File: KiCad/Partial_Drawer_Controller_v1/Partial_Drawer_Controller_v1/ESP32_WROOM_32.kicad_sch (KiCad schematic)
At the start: 41 parts, among them Q1 SS8050, Q2 2N7002T-7-F, Q3 2N7002T-7-F, Q5 SS8050, U6 CP2102N-Axx-xQFN28, U7 ESP32-WROOM-32E-N8, X1 USB-Micro

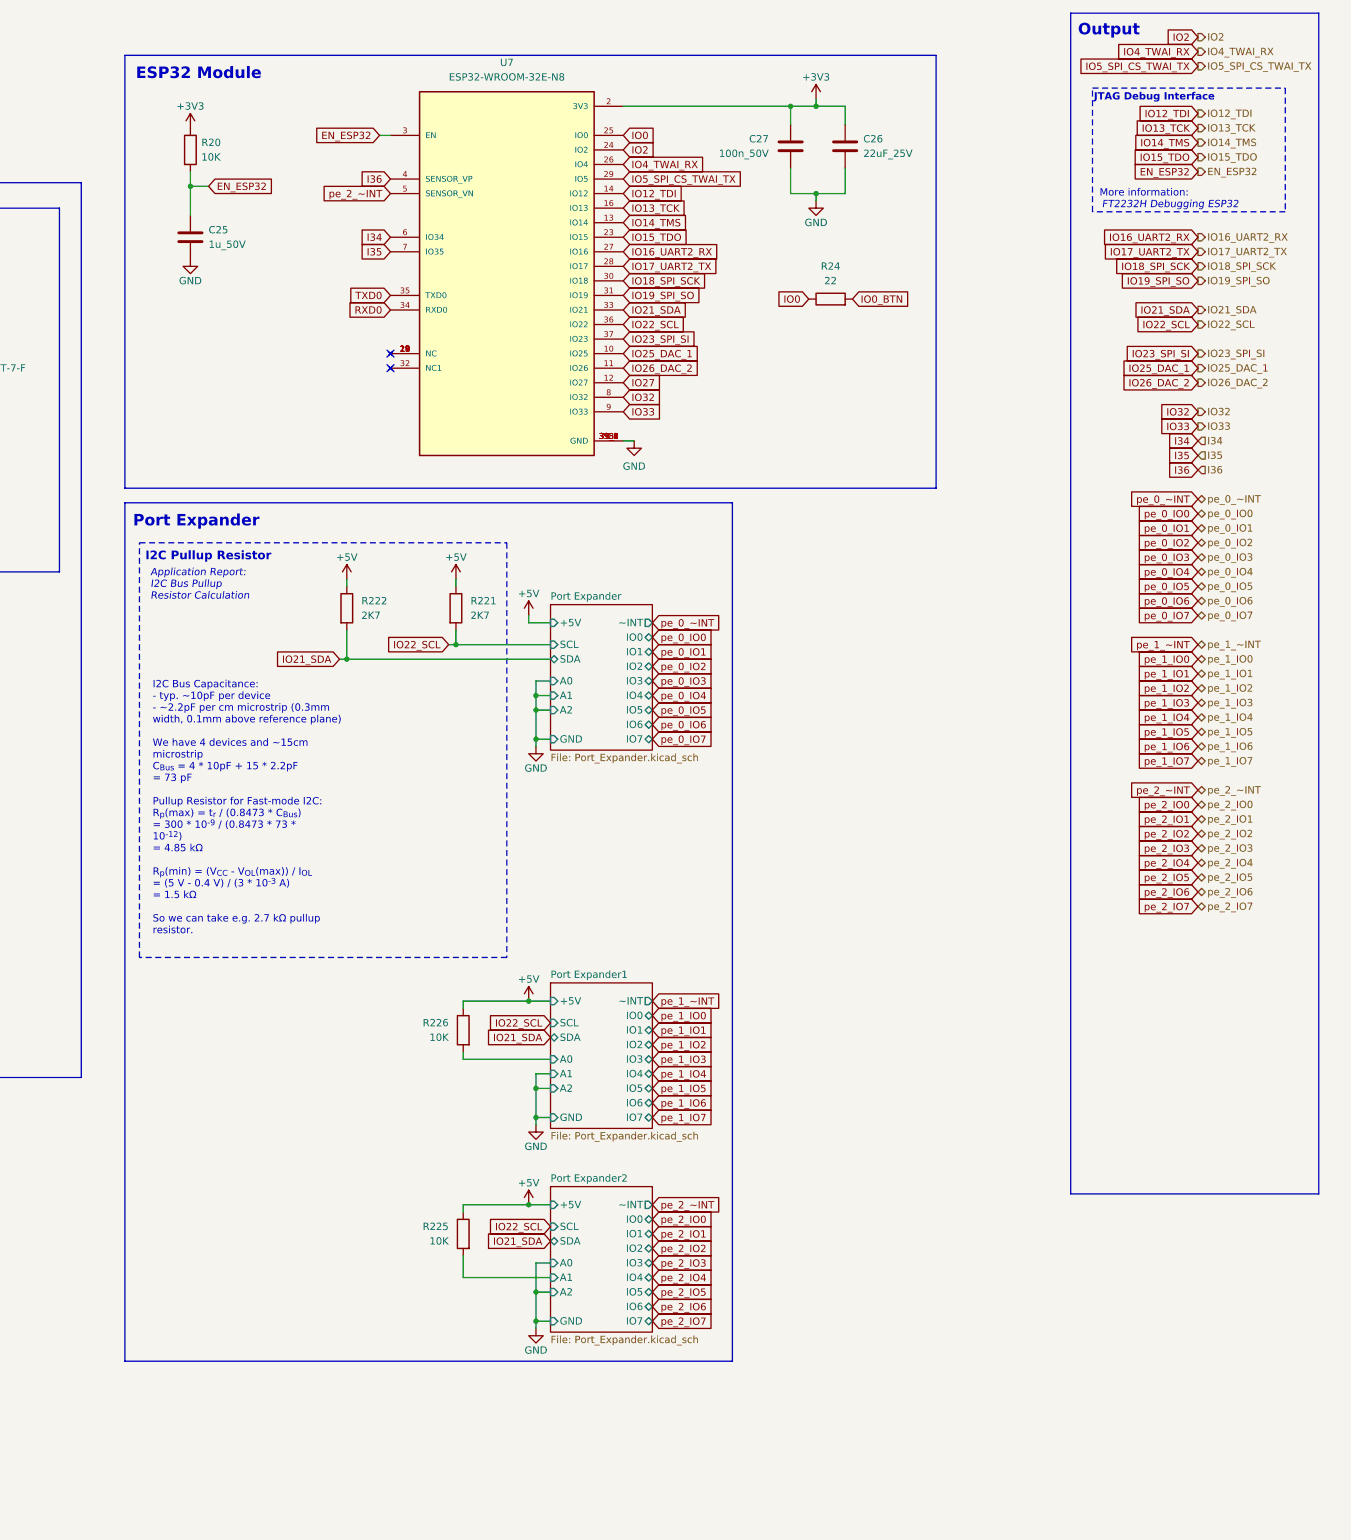
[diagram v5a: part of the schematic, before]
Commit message: feat: adds a lot of connectors and e-drawer support
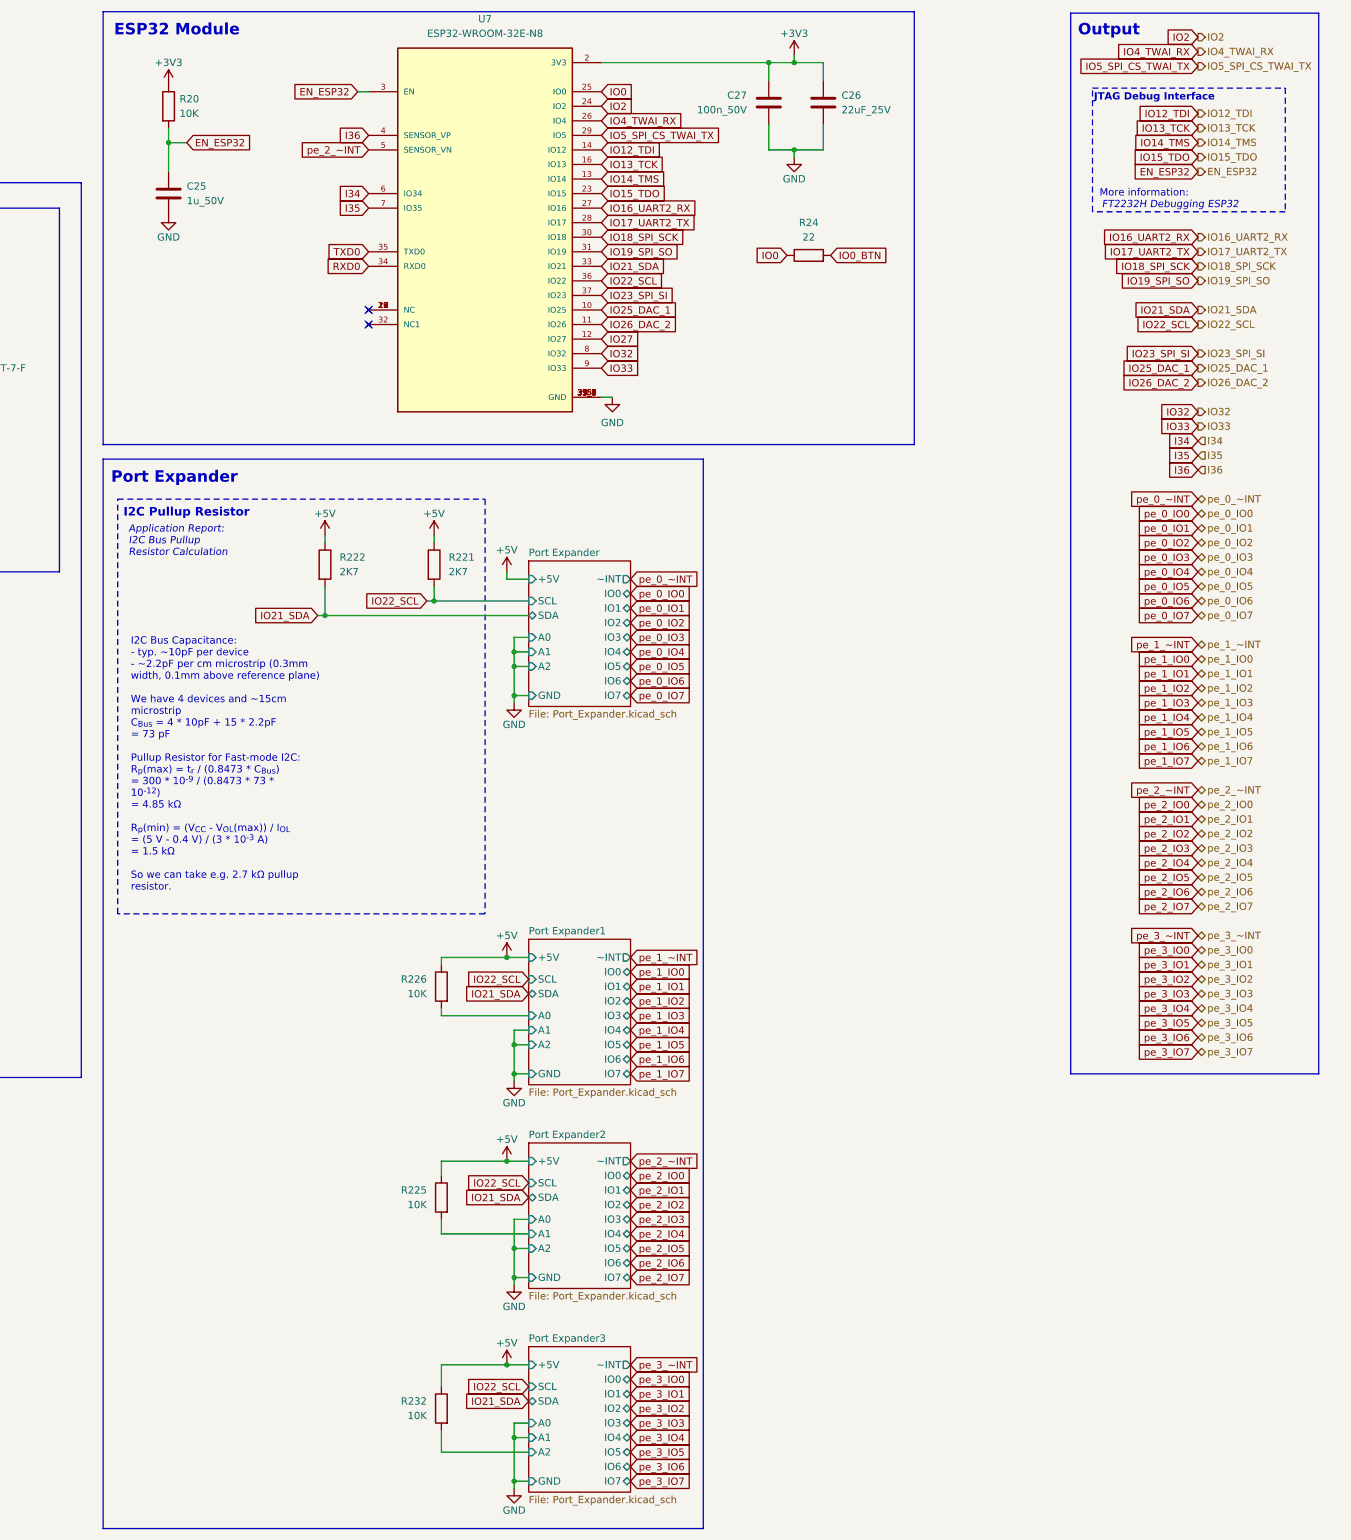
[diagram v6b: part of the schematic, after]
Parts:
- added R232: 10K, Resistor_SMD:R_0402_1005Metric, symbol _R_0402:10K
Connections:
- net +5V: now also R232.1
- new net Port Expander3/A2: R232.2
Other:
- added sheet Port Expander3 (Port_Expander.kicad_sch)
- moved on the sheet: C25, C26, C27, R20, R221, R222, R225, R226, R24, U7

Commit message: feat: finishing first draft for `partial_drawer_controller_v1` schematic
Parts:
- removed R226, R232: 10K, Resistor_SMD:R_0402_1005Metric, symbol _R_0402:10K
- added R224: 10K, Resistor_SMD:R_0402_1005Metric, symbol _R_0402:10K
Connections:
- net +5V: now also R224.1
- net Port Expander1/A0: now also R224.2
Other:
- removed sheet Port Expander3
- sheet Port Expander ports: added IO0_0, IO0_1, IO0_2, IO0_3, IO0_4, IO0_5, IO0_6, IO0_7, IO1_0, IO1_1, IO1_2, IO1_3, IO1_4, IO1_5, IO1_6, IO1_7; removed IO0, IO1, IO2, IO3, IO4, IO5, IO6, IO7
- sheet Port Expander1 ports: added IO0_0, IO0_1, IO0_2, IO0_3, IO0_4, IO0_5, IO0_6, IO0_7, IO1_0, IO1_1, IO1_2, IO1_3, IO1_4, IO1_5, IO1_6, IO1_7; removed IO0, IO1, IO2, IO3, IO4, IO5, IO6, IO7
- sheet Port Expander2 ports: added IO0_0, IO0_1, IO0_2, IO0_3, IO0_4, IO0_5, IO0_6, IO0_7, IO1_0, IO1_1, IO1_2, IO1_3, IO1_4, IO1_5, IO1_6, IO1_7; removed IO0, IO1, IO2, IO3, IO4, IO5, IO6, IO7

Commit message: feat: progress in routing - about 80% done
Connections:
- net pe_2_~INT: no longer U7.5 (SENSOR_VN)
- new net I39: U7.5 (SENSOR_VN)
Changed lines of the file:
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@@
 		)
 	)
-	(global_label "pe_2_~INT"
-		(shape input)
-		(at 240.03 38.1 180)
-		(fields_autoplaced yes)
-		(effects
-			(font
-				(size 1.27 1.27)
-			)
-			(justify right)
-		)
-		(property "Intersheetrefs" "${INTERSHEET_REFS}"
-			(at 227.9319 38.1 0)
-			(effects
-				(font
-					(size 1.27 1.27)
-				)
-				(justify right)
-				(hide yes)
-			)
-		)
-	)
 	(global_label "pe_1_IO1_3"
 		(shape input)
@@
 	(global_label "IO32"
 		(shape input)
-		(at 384.81 83.82 180)
+		(at 384.81 82.55 180)
 		(fields_autoplaced yes)
 		(effects
@@
 		)
 		(property "Intersheetrefs" "${INTERSHEET_REFS}"
-			(at 377.5499 83.82 0)
+			(at 377.5499 82.55 0)
 			(effects
 				(font
@@
 	(global_label "I35"
 		(shape input)
-		(at 384.81 91.44 180)
+		(at 384.81 90.17 180)
 		(fields_autoplaced yes)
 		(effects
@@
 		)
 		(property "Intersheetrefs" "${INTERSHEET_REFS}"
-			(at 378.8804 91.44 0)
+			(at 378.8804 90.17 0)
 			(effects
 				(font
@@
 	(global_label "I34"
 		(shape input)
-		(at 384.81 88.9 180)
+		(at 384.81 87.63 180)
 		(fields_autoplaced yes)
 		(effects
@@
 		)
 		(property "Intersheetrefs" "${INTERSHEET_REFS}"
-			(at 378.8804 88.9 0)
+			(at 378.8804 87.63 0)
 			(effects
 				(font
@@
 	(global_label "I36"
 		(shape input)
-		(at 384.81 93.98 180)
+		(at 384.81 92.71 180)
 		(fields_autoplaced yes)
 		(effects
@@
 		)
 		(property "Intersheetrefs" "${INTERSHEET_REFS}"
-			(at 378.8804 93.98 0)
+			(at 378.8804 92.71 0)
 			(effects
 				(font
@@
 		)
 	)
+	(global_label "I39"
+		(shape input)
+		(at 384.81 95.25 180)
+		(fields_autoplaced yes)
+		(effects
+			(font
+				(size 1.27 1.27)
+			)
+			(justify right)
+		)
+		(property "Intersheetrefs" "${INTERSHEET_REFS}"
+			(at 378.801 95.25 0)
+			(effects
+				(font
+					(size 1.27 1.27)
+				)
+				(justify right)
+				(hide yes)
+			)
+		)
+	)
 	(global_label "IO21_SDA"
 		(shape input)
@@
 	(global_label "IO33"
 		(shape input)
-		(at 384.81 86.36 180)
+		(at 384.81 85.09 180)
 		(fields_autoplaced yes)
 		(effects
@@
 		)
 		(property "Intersheetrefs" "${INTERSHEET_REFS}"
-			(at 377.5499 86.36 0)
+			(at 377.5499 85.09 0)
 			(effects
 				(font
@@
 		)
 	)
+	(global_label "I39"
+		(shape input)
+		(at 240.03 38.1 180)
+		(fields_autoplaced yes)
+		(effects
+			(font
+				(size 1.27 1.27)
+			)
+			(justify right)
+		)
+		(property "Intersheetrefs" "${INTERSHEET_REFS}"
+			(at 234.021 38.1 0)
+			(effects
+				(font
+					(size 1.27 1.27)
+				)
+				(justify right)
+				(hide yes)
+			)
+		)
+	)
 	(global_label "USB_D-"
 		(shape input)
@@
 	(hierarchical_label "IO33"
 		(shape output)
-		(at 384.81 86.36 0)
+		(at 384.81 85.09 0)
 		(fields_autoplaced yes)
 		(effects
@@
 		)
 	)
+	(hierarchical_label "I39"
+		(shape input)
+		(at 384.81 95.25 0)
+		(fields_autoplaced yes)
+		(effects
+			(font
+				(size 1.27 1.27)
+			)
+			(justify left)
+		)
+	)
 	(hierarchical_label "pe_1_IO0_1"
 		(shape bidirectional)
@@
 	(hierarchical_label "IO32"
 		(shape output)
-		(at 384.81 83.82 0)
+		(at 384.81 82.55 0)
 		(fields_autoplaced yes)
 		(effects
@@
 		)
 	)
-	(hierarchical_label "pe_2_IO0_6"
+	(hierarchical_label "pe_2_IO0_7"
 		(shape bidirectional)
 		(at 384.81 210.82 0)
@@
 	(hierarchical_label "I36"
 		(shape input)
-		(at 384.81 93.98 0)
+		(at 384.81 92.71 0)
 		(fields_autoplaced yes)
 		(effects
@@
 	(hierarchical_label "I34"
 		(shape input)
-		(at 384.81 88.9 0)
+		(at 384.81 87.63 0)
 		(fields_autoplaced yes)
 		(effects
@@
 	(hierarchical_label "I35"
 		(shape input)
-		(at 384.81 91.44 0)
+		(at 384.81 90.17 0)
 		(fields_autoplaced yes)
 		(effects
